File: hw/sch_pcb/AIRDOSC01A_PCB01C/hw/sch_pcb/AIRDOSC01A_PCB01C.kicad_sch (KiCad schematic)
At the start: 39 parts, among them J1 HEADER_2x01_PARALLEL, J10 HEADER_2x01_PARALLEL, J2 HEADER_2x01_PARALLEL, J3 HEADER_2x01_PARALLEL, J4 HEADER_2x01_PARALLEL, J5 HEADER_2x01_PARALLEL, J6 HEADER_2x01_PARALLEL, J7 HEADER_2x01_PARALLEL, J8 HEADER_2x01_PARALLEL, J9 HEADER_2x01_PARALLEL, M1 HOLE, M2 HOLE, M3 HOLE, M4 HOLE, U1 MICROFC-60035-SMT-TR(1), U2 OPA836IDB

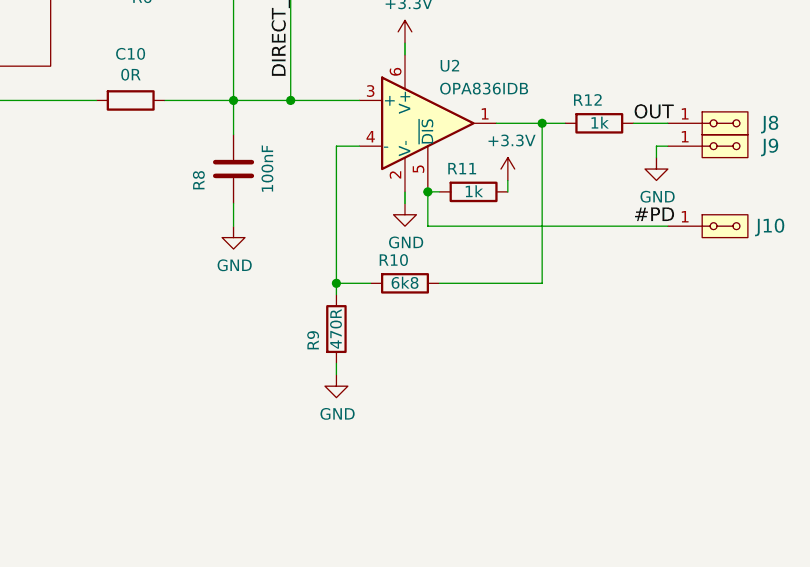
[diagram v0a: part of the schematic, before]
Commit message: Change R10 from 6k8 to 12k
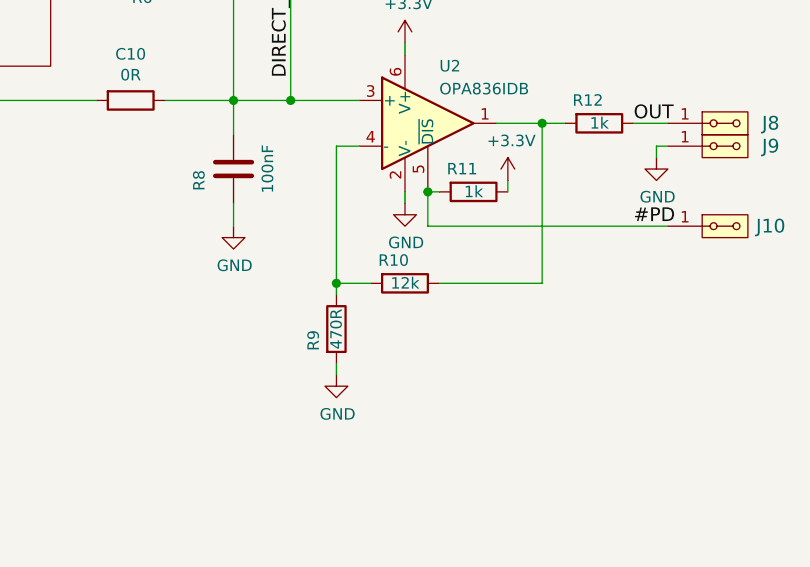
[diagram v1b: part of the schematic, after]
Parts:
- R10: value 6k8 -> 12k; UST_ID 5c70984612875079b91f899a -> 5c70984612875079b91f89a1
- U1: UST_ID (none) -> 60f907411287500165a96c1e
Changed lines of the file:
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@@
-(kicad_sch (version 20210406) (generator eeschema)
+(kicad_sch (version 20210621) (generator eeschema)
   (paper "A4")
   (title_block
@@
     (in_bom yes) (on_board yes)
     (property "Reference" "R10" (id 0) (at 201.93 113.03 90))
-    (property "Value" "6k8" (id 1) (at 203.2 115.57 90))
+    (property "Value" "12k" (id 1) (at 203.2 115.57 90))
     (property "Footprint" "Mlab_R:SMD-0805" (id 2) (at 203.2 113.792 90)
       (effects (font (size 1.27 1.27)) hide)
@@
       (effects (font (size 1.27 1.27)) hide)
     )
-    (property "UST_ID" "5c70984612875079b91f899a" (id 4) (at 203.2 115.57 0)
+    (property "UST_ID" "5c70984612875079b91f89a1" (id 4) (at 203.2 115.57 0)
       (effects (font (size 1.27 1.27)) hide)
     )
@@
       (effects (font (size 1.524 1.524)) hide)
     )
+    (property "UST_ID" "60f907411287500165a96c1e" (id 4) (at 154.94 83.82 0)
+      (effects (font (size 1.27 1.27)) hide)
+    )
     (pin "1")
     (pin "2")
@@
     )
     (path "/00000000-0000-0000-0000-00005c6ff14e"
-      (reference "R10") (unit 1) (value "6k8") (footprint "Mlab_R:SMD-0805")
+      (reference "R10") (unit 1) (value "12k") (footprint "Mlab_R:SMD-0805")
     )
     (path "/00000000-0000-0000-0000-00005c6f9be2"
